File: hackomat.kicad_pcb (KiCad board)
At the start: 2 copper layers, 95 x 95 mm, 54 parts, among them IC1 MOC3021M, IC10 MOC3021M, IC11 MOC3021M, IC12 MOC3021M, IC13 MOC3021M, IC14 MOC3021M, IC15 MOC3021M, IC16 MOC3021M, IC17 MOC3021M, IC18 MOC3021M, IC19 MOC3021M, IC2 MOC3021M, IC20 MOC3021M, IC21 MOC3021M, IC22 MOC3021M, IC23 MOC3021M, IC24 MOC3021M, IC25 MOC3021M, IC26 MOC3021M, IC27 MOC3021M, IC28 MOC3021M, IC29 MOC3021M, IC3 MOC3021M, IC30 MOC3021M, IC31 MOC3021M, IC32 MOC3021M, IC33 MOC3021M, IC34 MOC3021M, IC35 MOC3021M, IC36 MOC3021M, IC37 MOC3021M, IC38 MOC3021M, IC39 MOC3021M, IC4 MOC3021M, IC40 MOC3021M, IC41 MOC3021M, IC42 MOC3021M, IC5 MOC3021M, IC6 MOC3021M, IC7 MOC3021M, IC8 MOC3021M, IC9 MOC3021M, J1 RJ45, P1 CONN_02X22, P2 CONN_02X08, P35 CONN_01X01, P36 CONN_01X01, P42 CONN_01X01

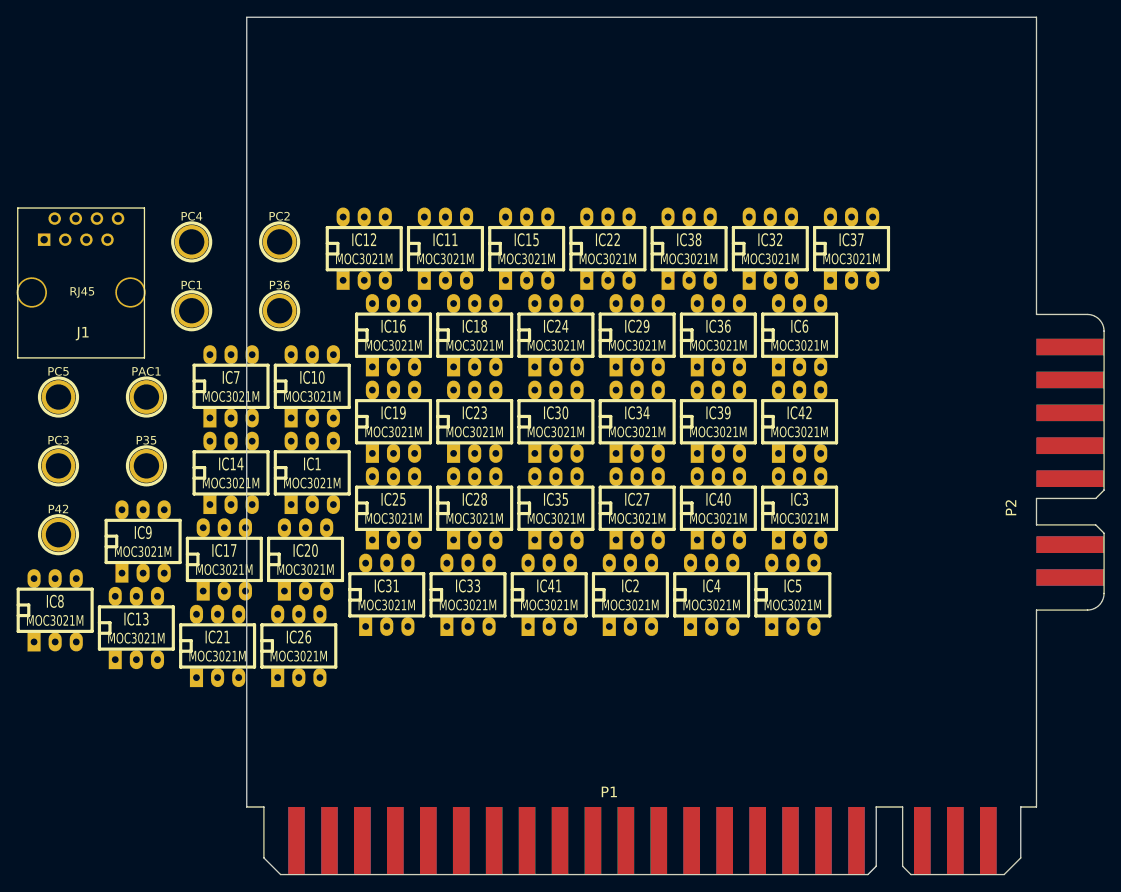
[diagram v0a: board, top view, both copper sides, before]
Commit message: move edge connectors to make entire board under 100x100mm
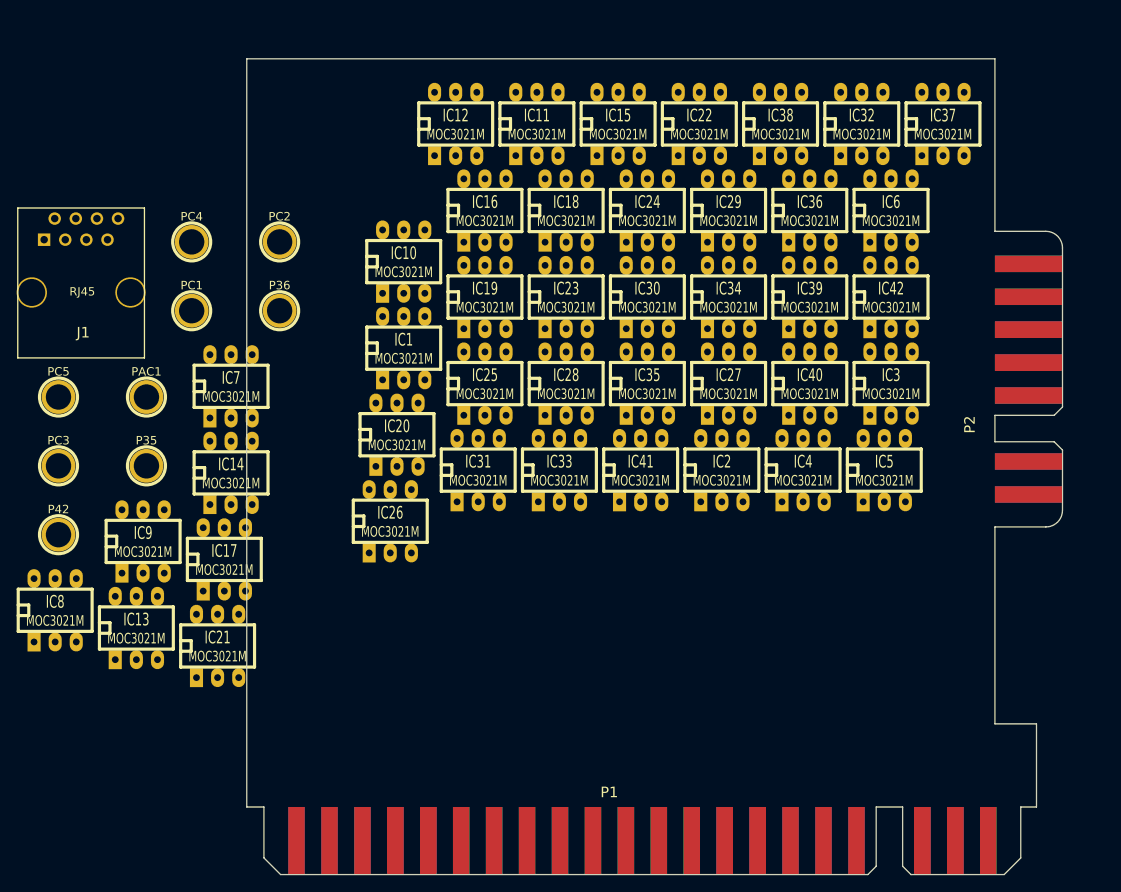
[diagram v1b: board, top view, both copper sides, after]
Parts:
- moved IC20 18.6 mm to (178.1, 115.2)
- moved IC26 18.6 mm to (177.3, 125.6)
- moved IC1 18.6 mm to (178.9, 104.8)
- moved IC10 18.6 mm to (178.9, 94.4)
- moved IC11 18.6 mm to (194.9, 77.8)
- moved IC12 18.6 mm to (185.1, 77.8)
- moved IC15 18.6 mm to (204.7, 77.8)
- moved IC16 18.6 mm to (188.7, 88.2)
- moved IC18 18.6 mm to (198.4, 88.2)
- moved IC19 18.6 mm to (188.7, 98.7)
- moved IC2 18.6 mm to (217.2, 119.5)
- moved IC22 18.6 mm to (214.5, 77.8)
- moved IC23 18.6 mm to (198.4, 98.7)
- moved IC24 18.6 mm to (208.2, 88.2)
- moved IC25 18.6 mm to (188.7, 109.1)
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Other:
- board size 95 x 95 mm -> 95 x 90 mm
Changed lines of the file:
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@@
     (area 112.979999 64.719999 255.320001 161.340001)
     (thickness 1.6)
-    (drawings 10)
+    (drawings 12)
     (tracks 0)
     (zones 0)
@@
     (pad_to_mask_clearance 0)
     (aux_axis_origin 0 0)
-    (visible_elements 7FFFEF7F)
+    (visible_elements 7FFFFF7F)
     (pcbplotparams
       (layerselection 0x01030_80000001)
@@
   )
   (module Sockets_DIP:DIP-6__300_ELL (layer F.Cu)
-    (at 167.899501 119.807)
+    (at 178.899501 104.807)
     (descr "6 pins DIL package, elliptical pads")
     (tags DIL)
@@
   )
   (module Sockets_DIP:DIP-6__300_ELL (layer F.Cu)
-    (at 206.169501 134.477)
+    (at 217.169501 119.477)
     (descr "6 pins DIL package, elliptical pads")
     (tags DIL)
@@
   )
   (module Sockets_DIP:DIP-6__300_ELL (layer F.Cu)
-    (at 226.519501 124.067)
+    (at 237.519501 109.067)
     (descr "6 pins DIL package, elliptical pads")
     (tags DIL)
@@
   )
   (module Sockets_DIP:DIP-6__300_ELL (layer F.Cu)
-    (at 215.939501 134.477)
+    (at 226.939501 119.477)
     (descr "6 pins DIL package, elliptical pads")
     (tags DIL)
@@
   )
   (module Sockets_DIP:DIP-6__300_ELL (layer F.Cu)
-    (at 225.709501 134.477)
+    (at 236.709501 119.477)
     (descr "6 pins DIL package, elliptical pads")
     (tags DIL)
@@
   )
   (module Sockets_DIP:DIP-6__300_ELL (layer F.Cu)
-    (at 226.519501 103.247)
+    (at 237.519501 88.247)
     (descr "6 pins DIL package, elliptical pads")
     (tags DIL)
@@
   )
   (module Sockets_DIP:DIP-6__300_ELL (layer F.Cu)
-    (at 167.899501 109.397)
+    (at 178.899501 94.397)
     (descr "6 pins DIL package, elliptical pads")
     (tags DIL)
@@
   )
   (module Sockets_DIP:DIP-6__300_ELL (layer F.Cu)
-    (at 183.919501 92.837)
+    (at 194.919501 77.837)
     (descr "6 pins DIL package, elliptical pads")
     (tags DIL)
@@
   )
   (module Sockets_DIP:DIP-6__300_ELL (layer F.Cu)
-    (at 174.149501 92.837)
+    (at 185.149501 77.837)
     (descr "6 pins DIL package, elliptical pads")
     (tags DIL)
@@
   )
   (module Sockets_DIP:DIP-6__300_ELL (layer F.Cu)
-    (at 193.689501 92.837)
+    (at 204.689501 77.837)
     (descr "6 pins DIL package, elliptical pads")
     (tags DIL)
@@
   )
   (module Sockets_DIP:DIP-6__300_ELL (layer F.Cu)
-    (at 177.669501 103.247)
+    (at 188.669501 88.247)
     (descr "6 pins DIL package, elliptical pads")
     (tags DIL)
@@
   )
   (module Sockets_DIP:DIP-6__300_ELL (layer F.Cu)
-    (at 187.439501 103.247)
+    (at 198.439501 88.247)
     (descr "6 pins DIL package, elliptical pads")
     (tags DIL)
@@
   )
   (module Sockets_DIP:DIP-6__300_ELL (layer F.Cu)
-    (at 177.669501 113.657)
+    (at 188.669501 98.657)
     (descr "6 pins DIL package, elliptical pads")
     (tags DIL)
@@
   )
   (module Sockets_DIP:DIP-6__300_ELL (layer F.Cu)
-    (at 167.089501 130.217)
+    (at 178.089501 115.217)
     (descr "6 pins DIL package, elliptical pads")
     (tags DIL)
@@
   )
   (module Sockets_DIP:DIP-6__300_ELL (layer F.Cu)
-    (at 203.459501 92.837)
+    (at 214.459501 77.837)
     (descr "6 pins DIL package, elliptical pads")
     (tags DIL)
@@
   )
   (module Sockets_DIP:DIP-6__300_ELL (layer F.Cu)
-    (at 187.439501 113.657)
+    (at 198.439501 98.657)
     (descr "6 pins DIL package, elliptical pads")
     (tags DIL)
@@
   )
   (module Sockets_DIP:DIP-6__300_ELL (layer F.Cu)
-    (at 197.209501 103.247)
+    (at 208.209501 88.247)
     (descr "6 pins DIL package, elliptical pads")
     (tags DIL)
@@
   )
   (module Sockets_DIP:DIP-6__300_ELL (layer F.Cu)
-    (at 177.669501 124.067)
+    (at 188.669501 109.067)
     (descr "6 pins DIL package, elliptical pads")
     (tags DIL)
@@
   )
   (module Sockets_DIP:DIP-6__300_ELL (layer F.Cu)
-    (at 166.279501 140.627)
+    (at 177.279501 125.627)
     (descr "6 pins DIL package, elliptical pads")
     (tags DIL)
@@
   )
   (module Sockets_DIP:DIP-6__300_ELL (layer F.Cu)
-    (at 206.979501 124.067)
+    (at 217.979501 109.067)
     (descr "6 pins DIL package, elliptical pads")
     (tags DIL)
@@
   )
   (module Sockets_DIP:DIP-6__300_ELL (layer F.Cu)
-    (at 187.439501 124.067)
+    (at 198.439501 109.067)
     (descr "6 pins DIL package, elliptical pads")
     (tags DIL)
@@
   )
   (module Sockets_DIP:DIP-6__300_ELL (layer F.Cu)
-    (at 206.979501 103.247)
+    (at 217.979501 88.247)
     (descr "6 pins DIL package, elliptical pads")
     (tags DIL)
@@
   )
   (module Sockets_DIP:DIP-6__300_ELL (layer F.Cu)
-    (at 197.209501 113.657)
+    (at 208.209501 98.657)
     (descr "6 pins DIL package, elliptical pads")
     (tags DIL)
@@
   )
   (module Sockets_DIP:DIP-6__300_ELL (layer F.Cu)
-    (at 176.859501 134.477)
+    (at 187.859501 119.477)
     (descr "6 pins DIL package, elliptical pads")
     (tags DIL)
@@
   )
   (module Sockets_DIP:DIP-6__300_ELL (layer F.Cu)
-    (at 222.999501 92.837)
+    (at 233.999501 77.837)
     (descr "6 pins DIL package, elliptical pads")
     (tags DIL)
@@
   )
   (module Sockets_DIP:DIP-6__300_ELL (layer F.Cu)
-    (at 186.629501 134.477)
+    (at 197.629501 119.477)
     (descr "6 pins DIL package, elliptical pads")
     (tags DIL)
@@
   )
   (module Sockets_DIP:DIP-6__300_ELL (layer F.Cu)
-    (at 206.979501 113.657)
+    (at 217.979501 98.657)
     (descr "6 pins DIL package, elliptical pads")
     (tags DIL)
@@
   )
   (module Sockets_DIP:DIP-6__300_ELL (layer F.Cu)
-    (at 197.209501 124.067)
+    (at 208.209501 109.067)
     (descr "6 pins DIL package, elliptical pads")
     (tags DIL)
@@
   )
   (module Sockets_DIP:DIP-6__300_ELL (layer F.Cu)
-    (at 216.749501 103.247)
+    (at 227.749501 88.247)
     (descr "6 pins DIL package, elliptical pads")
     (tags DIL)
@@
   )
   (module Sockets_DIP:DIP-6__300_ELL (layer F.Cu)
-    (at 232.769501 92.837)
+    (at 243.769501 77.837)
     (descr "6 pins DIL package, elliptical pads")
     (tags DIL)
@@
   )
   (module Sockets_DIP:DIP-6__300_ELL (layer F.Cu)
-    (at 213.229501 92.837)
+    (at 224.229501 77.837)
     (descr "6 pins DIL package, elliptical pads")
     (tags DIL)
@@
   )
   (module Sockets_DIP:DIP-6__300_ELL (layer F.Cu)
-    (at 216.749501 113.657)
+    (at 227.749501 98.657)
     (descr "6 pins DIL package, elliptical pads")
     (tags DIL)
@@
   )
   (module Sockets_DIP:DIP-6__300_ELL (layer F.Cu)
-    (at 216.749501 124.067)
+    (at 227.749501 109.067)
     (descr "6 pins DIL package, elliptical pads")
     (tags DIL)
@@
   )
   (module Sockets_DIP:DIP-6__300_ELL (layer F.Cu)
-    (at 196.399501 134.477)
+    (at 207.399501 119.477)
     (descr "6 pins DIL package, elliptical pads")
     (tags DIL)
@@
   )
   (module Sockets_DIP:DIP-6__300_ELL (layer F.Cu)
-    (at 226.519501 113.657)
+    (at 237.519501 98.657)
     (descr "6 pins DIL package, elliptical pads")
     (tags DIL)
@@
   )
   (module euro:euro16 (layer F.Cu)
-    (at 259.08 132.4 90)
+    (at 254.08 122.4 90)
     (descr "card-edge euro 3.96mm snackshop 2 vending machine")
     (tags "CONN CARD EDGE EURO")
@@
       (net 60 "Net-(P2-Pad16)"))
   )
+  (gr_line (start 250.016 126.3116) (end 250.016 150) (angle 90) (layer Edge.Cuts) (width 0.15))
+  (gr_line (start 250.016 150) (end 255.016 150) (angle 90) (layer Edge.Cuts) (width 0.15))
   (gr_line (start 160.016 160) (end 162.0852 160) (angle 90) (layer Edge.Cuts) (width 0.15))
   (gr_text "166.000,164.064\n162.0852,160.000" (at 155 165) (layer Dwgs.User)
@@
     (effects (font (size 1 1) (thickness 0.1)))
   )
-  (gr_line (start 255.016 65) (end 255.016 100.7516) (angle 90) (layer Edge.Cuts) (width 0.15))
+  (gr_line (start 250.016 70) (end 250.016 90.7516) (angle 90) (layer Edge.Cuts) (width 0.15))
   (gr_text "259.08, 152.4\n255.016, 120.7516" (at 265.43 118.11) (layer Dwgs.User)
     (effects (font (size 1 1) (thickness 0.1)))
@@
   )
   (gr_line (start 253.1252 160) (end 255.016 160) (angle 90) (layer Edge.Cuts) (width 0.15))
-  (gr_line (start 160.016 65) (end 160.016 160) (angle 90) (layer Edge.Cuts) (width 0.15))
-  (gr_line (start 255.016 136.3116) (end 255.016 160) (angle 90) (layer Edge.Cuts) (width 0.15))
-  (gr_line (start 160.016 65) (end 255.016 65) (angle 90) (layer Edge.Cuts) (width 0.15))
+  (gr_line (start 160.016 70) (end 160.016 160) (angle 90) (layer Edge.Cuts) (width 0.15))
+  (gr_line (start 255.016 150) (end 255.016 160) (angle 90) (layer Edge.Cuts) (width 0.15))
+  (gr_line (start 160.016 70) (end 250.016 70) (angle 90) (layer Edge.Cuts) (width 0.15))
 )

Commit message: place all triacs and other parts on board in order
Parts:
- PC1, PC2, PC3, PC4, PC5: footprint Connect:1pin -> Pin_Headers:Pin_Header_Straight_1x01
- moved PC3 118.7 mm to (247.7, 74.9)
- moved PC5 116.7 mm to (247.7, 72.4)
- moved P42 115.3 mm to (238.8, 72.4)
- moved P35 104.1 mm to (245.1, 156.2)
- moved P36 103.8 mm to (251.5, 156.2)
- moved PC1 97.0 mm to (247.7, 77.5)
- moved PC4 93.3 mm to (245.1, 74.9)
- moved PC2 82.4 mm to (245.1, 77.5)
- moved IC6 78.5 mm to (190.5, 151.1), turned to 90 degrees
- moved IC32 74.8 mm to (228.6, 152.4), turned to 90 degrees
- moved IC5 72.9 mm to (168.9, 92.7), turned to 270 degrees
- moved IC3 70.0 mm to (168.9, 123.2), turned to 270 degrees
- moved J1 66.5 mm to (201.9, 73.7), turned to 180 degrees
- moved IC22 66.1 mm to (207.0, 143.5), turned to 270 degrees
- moved IC12 65.9 mm to (190.5, 143.5), turned to 90 degrees
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
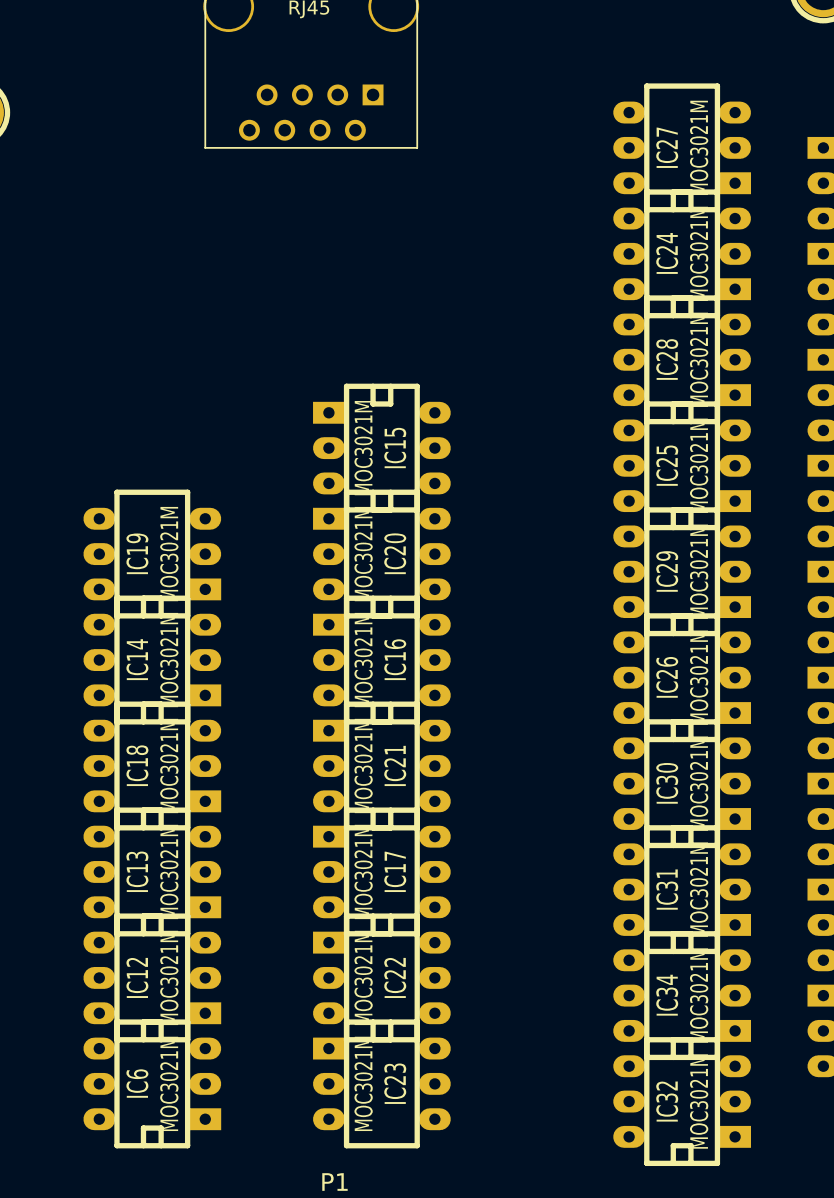
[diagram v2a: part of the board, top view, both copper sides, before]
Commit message: move triacs to a more sensible, more sequential arrangement
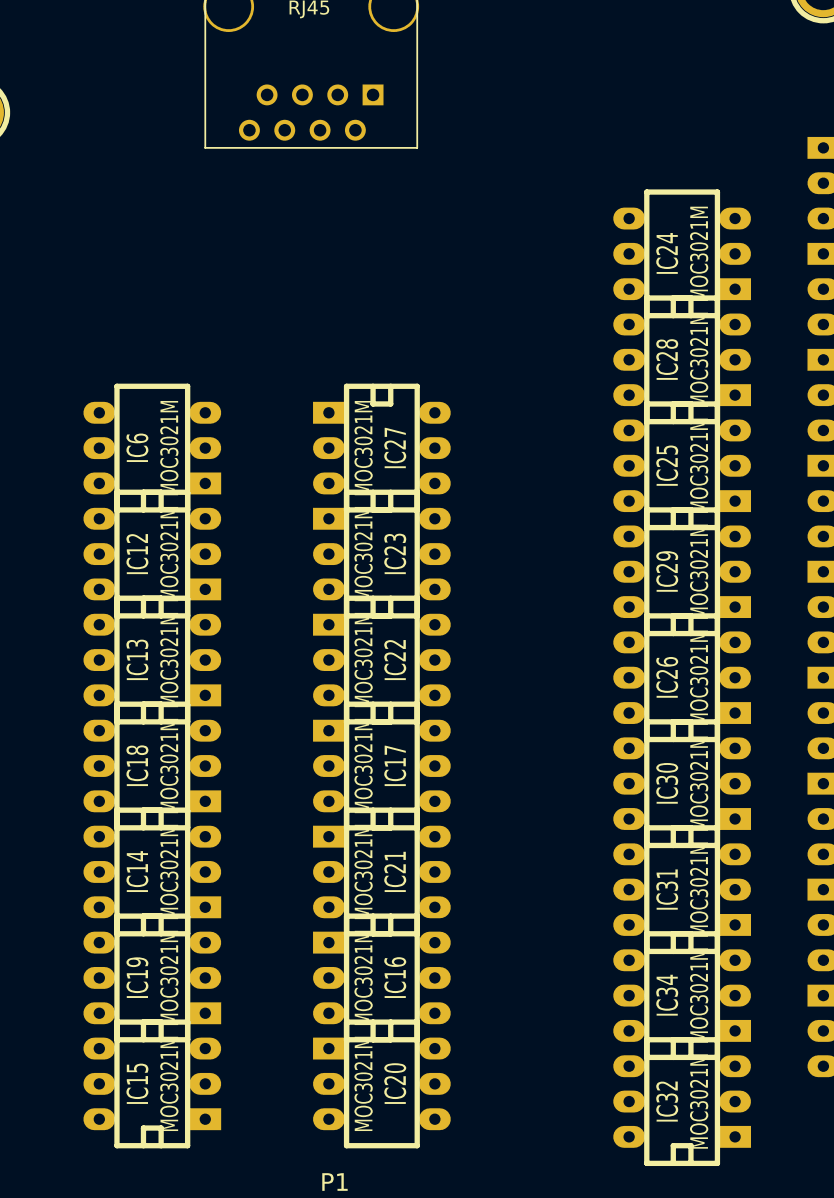
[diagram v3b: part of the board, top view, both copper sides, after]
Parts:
- moved IC15 48.6 mm to (190.5, 151.1), turned to 90 degrees
- moved IC6 45.7 mm to (190.5, 105.4)
- moved IC20 38.1 mm to (207.0, 151.1)
- moved IC23 38.1 mm to (207.0, 113.0)
- moved IC27 30.5 mm to (207.0, 105.4), turned to 270 degrees
- moved IC12 30.5 mm to (190.5, 113.0)
- moved IC19 30.5 mm to (190.5, 143.5)
- moved IC16 22.9 mm to (207.0, 143.5)
- moved IC22 22.9 mm to (207.0, 120.7)
- moved IC13 15.2 mm to (190.5, 120.7)
- moved IC14 15.2 mm to (190.5, 135.9)
- moved IC17 7.62 mm to (207.0, 128.3)
- moved IC21 7.62 mm to (207.0, 135.9)
